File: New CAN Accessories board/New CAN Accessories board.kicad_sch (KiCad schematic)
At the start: 76 parts, among them J1 39301040, J10 39301060, J2 39301040, J3 39301040, J4 39301040, J5 39301040, J6 39301040, J7 39301040, J8 39301040, J9 39301060, Q1 IRLML6344TRPBF, Q2 IRLML6344TRPBF, Q3 IRLML6344TRPBF, Q4 IRLML6344TRPBF, Q5 IRLML6344TRPBF, Q6 IRLML6344TRPBF, Q7 IRLML6344TRPBF, Q8 IRLML6344TRPBF, SW1 SW_DPDT_x2, SW3 SW_DPDT_x2, U1 NUCLEO_L432KC, U2 MCP2562FD-E_SN

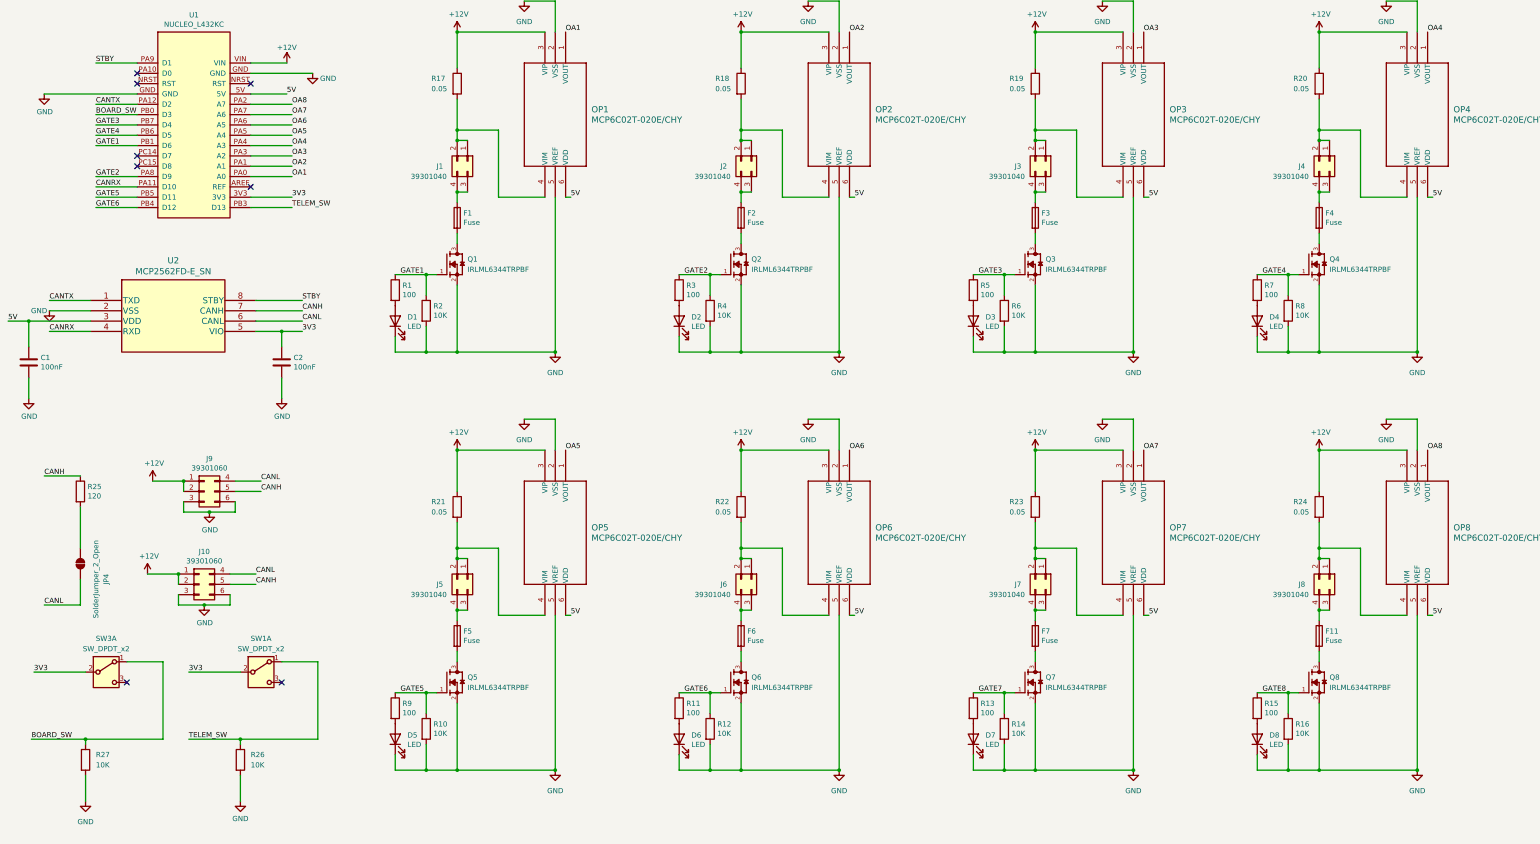
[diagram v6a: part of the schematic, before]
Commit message: Added decoupling caps on opamps, improved part designator labelling and naming
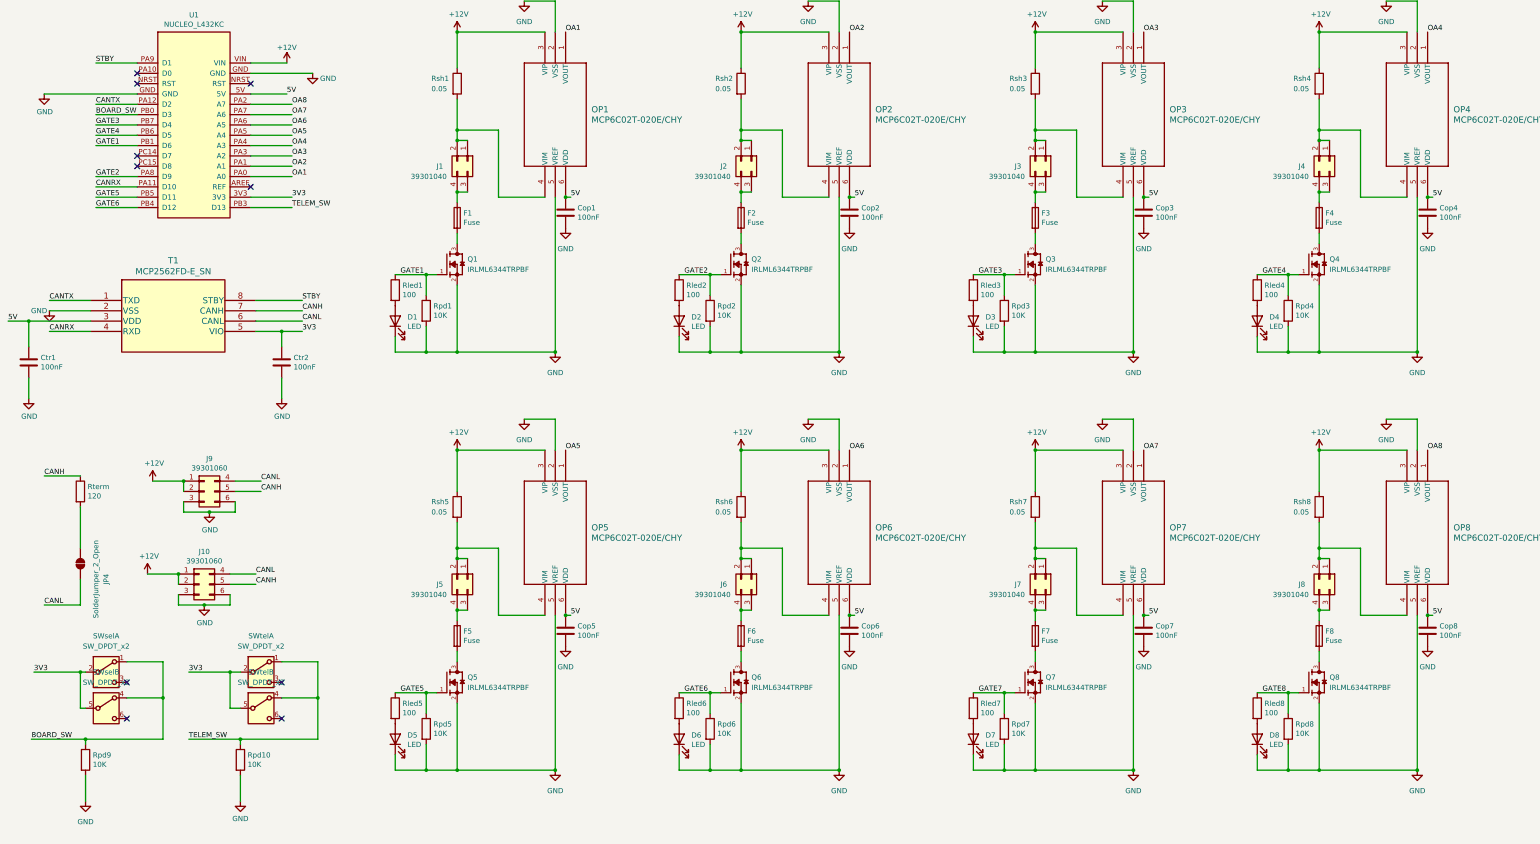
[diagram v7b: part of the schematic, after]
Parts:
- removed R10, R12, R14, R16, R26, R27, R4, R6, R8: 10K, Resistor_SMD:R_0805_2012Metric, symbol Device:R
- removed R11, R13, R15, R3, R5, R7, R9: 100, Resistor_SMD:R_0805_2012Metric, symbol Device:R
- removed R18, R19, R20, R21, R22, R23, R24: 0.05, Resistor_SMD:R_2512_6332Metric_Pad1.40x3.35mm_HandSolder, symbol Device:R
- added Cop1, Cop2, Cop3, Cop4, Cop5, Cop6, Cop7, Cop8: 100nF, Capacitor_SMD:C_0805_2012Metric, symbol Device:C
- added Rled2, Rled3, Rled4, Rled5, Rled6, Rled7, Rled8: 100, Resistor_SMD:R_0805_2012Metric, symbol Device:R
- added Rpd10, Rpd2, Rpd3, Rpd4, Rpd5, Rpd6, Rpd7, Rpd8, Rpd9: 10K, Resistor_SMD:R_0805_2012Metric, symbol Device:R
- added Rsh2, Rsh3, Rsh4, Rsh5, Rsh6, Rsh7, Rsh8: 0.05, Resistor_SMD:R_2512_6332Metric_Pad1.40x3.35mm_HandSolder, symbol Device:R
- added unit 2 of SWsel
- added unit 2 of SWtel
- renumbered C1 to Ctr1, C2 to Ctr2, F11 to F8, R1 to Rled1, R2 to Rpd1, R17 to Rsh1, R25 to Rterm, SW3 to SWsel, SW1 to SWtel, U2 to T1
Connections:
- net +12V: now also Rsh2.1, Rsh3.1, Rsh4.1, Rsh5.1, Rsh6.1, Rsh7.1, Rsh8.1
- net 3V3: now also SWsel.5 (B), SWtel.5 (B)
- net 5V: now also Cop1.1, Cop2.1, Cop3.1, Cop4.1, Cop5.1, Cop6.1, Cop7.1, Cop8.1
- net BOARD_SW: now also Rpd9.1, SWsel.4 (A)
- net GATE2: now also Rled2.1, Rpd2.1
- net GATE3: now also Rled3.1, Rpd3.1
- net GATE4: now also Rled4.1, Rpd4.1
- net GATE5: now also Rled5.1, Rpd5.1
- net GATE6: now also Rled6.1, Rpd6.1
- net GATE7: now also Rled7.1, Rpd7.1
- net GATE8: now also Rled8.1, Rpd8.1
- net GND: now also Cop1.2, Cop2.2, Cop3.2, Cop4.2, Cop5.2, Cop6.2, Cop7.2, Cop8.2, Rpd10.2, Rpd2.2, Rpd3.2, Rpd4.2, Rpd5.2, Rpd6.2, Rpd7.2, Rpd8.2, Rpd9.2
- net TELEM_SW: now also Rpd10.1, SWtel.4 (A)
- net at J6.1 (Pin_1), J6.2 (Pin_2), OP6.4 (VIM): now also Rsh6.2
- net at J4.1 (Pin_1), J4.2 (Pin_2), OP4.4 (VIM): now also Rsh4.2
- net at J7.1 (Pin_1), J7.2 (Pin_2), OP7.4 (VIM): now also Rsh7.2
- net at D4.2 (A): now also Rled4.2
- net at J8.1 (Pin_1), J8.2 (Pin_2), OP8.4 (VIM): now also Rsh8.2
- net at D7.2 (A): now also Rled7.2
- net at J3.1 (Pin_1), J3.2 (Pin_2), OP3.4 (VIM): now also Rsh3.2
- net at D6.2 (A): now also Rled6.2
- net at D2.2 (A): now also Rled2.2
- net at J5.1 (Pin_1), J5.2 (Pin_2), OP5.4 (VIM): now also Rsh5.2
- net at J2.1 (Pin_1), J2.2 (Pin_2), OP2.4 (VIM): now also Rsh2.2
- net at D3.2 (A): now also Rled3.2
- net at D8.2 (A): now also Rled8.2
- net at D5.2 (A): now also Rled5.2
- no-connect marks 8 -> 10

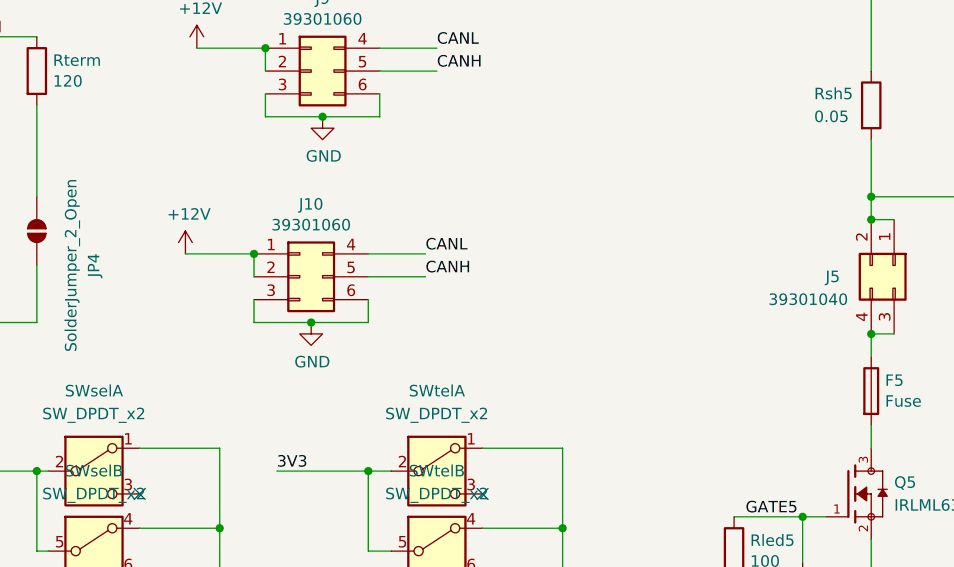
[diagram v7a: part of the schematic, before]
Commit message: split J10 into 2pin 12V connector and 4pin can connector
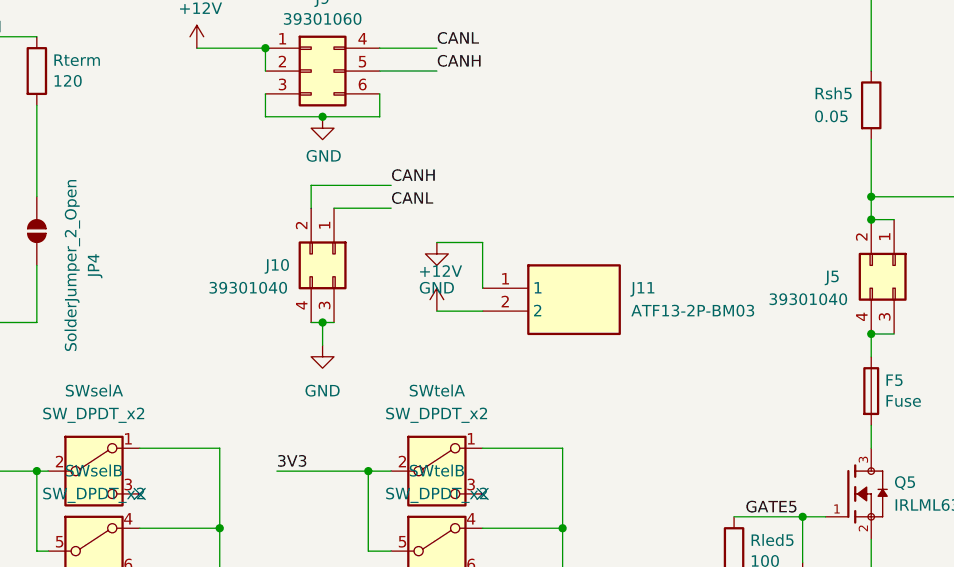
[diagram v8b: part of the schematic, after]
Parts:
- removed J10: 39301060, Connector_Molex:Molex_Mini-Fit_Jr_5569-06A2_2x03_P4.20mm_Horizontal, symbol Connector_Generic:Conn_02x03_Top_Bottom
- added J10: 39301040, Connector_Molex:Molex_Mini-Fit_Jr_5569-04A2_2x02_P4.20mm_Horizontal, symbol Connector_Generic:Conn_02x02_Top_Bottom
- added J11: ATF13-2P-BM03, footprint:ATF132PBM03, symbol ATF13-2P-BM03:ATF13-2P-BM03
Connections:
- net +12V: now also J11.2
- net CANH: now also J10.2 (Pin_2)
- net CANL: now also J10.1 (Pin_1)
- net GND: now also J10.3 (Pin_3), J10.4 (Pin_4), J11.1
